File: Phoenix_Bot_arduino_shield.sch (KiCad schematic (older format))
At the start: 14 parts

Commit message: Updated the Schematic with solenoids
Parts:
- removed J?: Conn_01x06_Male, symbol Conn_01x06_Male
- removed Q? (x6): Q_NMOS_GDS, symbol Q_NMOS_GDS
- added J?: Screw_Terminal_01x12, symbol Screw_Terminal_01x12
- added J? (x2): 1x8 Male, symbol Conn_01x08_Male
- added J? (x2): 1x8 Female, symbol Conn_01x08_Female
- added q?: solenoid_1, symbol Q_NMOS_DGS
- added q? (x2): solenoid_3, symbol Q_NMOS_DGS
- added q?: solenoid_4, symbol Q_NMOS_DGS
- added q?: solenoid_5, symbol Q_NMOS_DGS
- added q?: solenoid_6, symbol Q_NMOS_DGS
- J?: value Conn_01x08_Female -> On Board Supply
- J?: value Conn_01x08_Female -> Analog_Pin_1
- J?: value Conn_01x08_Female -> Analog_Pin_2
- J?: value Conn_02x18_Top_Bottom -> Digital_Pins
- J?: value Conn_01x08_Female -> Serial
- J?: value Conn_01x08_Female -> PWM_(6-1)
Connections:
- net labels added: +12V, +5V, 11, 7, 9, Ctrl_1, Ctrl_2, Ctrl_3, Ctrl_4, Ctrl_5, Ctrl_6, Drain_1, Drain_2, Drain_3, Drain_4, Drain_5, Drain_6, RX, TX
- net labels removed: 2, 4, 6
- wire segments 18 -> 87
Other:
- moved on the sheet: J?

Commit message: Updated the Schematic with Analog mapping, encoder, solenoid,  and servo
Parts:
- added J? (x2): Ground, symbol Conn_01x06_Male
- added J?: Servo_Power, symbol Conn_01x06_Male
- added J?: Servo_signal, symbol Conn_01x06_Male
- added J?: PWN(10-5), symbol Conn_01x10_Female
- added J?: ICSP, symbol Conn_02x03_Top_Bottom
- added J?: Encoder_Power, symbol Conn_01x06_Male
- added J?: Encoder_signal, symbol Conn_01x06_Male
- added J?: Analog_signal_female, symbol Conn_01x08_Female
- added J?: Analog_Power_female, symbol Conn_01x08_Female
- added J?: Ground, symbol Conn_01x08_Female
- added J?: Analog_signal_male, symbol Conn_01x08_Male
- added J?: Analog_signal_power, symbol Conn_01x08_Male
- added J?: Ground, symbol Conn_01x08_Male
- J?: value Conn_01x10_Female -> PWN(10-5)
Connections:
- net labels added: +3.3V, AREF, Analog_1, Analog_10, Analog_11, Analog_12, Analog_13, Analog_14, Analog_15, Analog_16, Analog_2, Analog_3, Analog_4, Analog_5, Analog_6, Analog_7, Analog_8, Analog_9, Encoder_1, Encoder_2, Encoder_3, Encoder_4, Encoder_5, Encoder_6, IOREF, Reset, SCL, SDA, Servo_1, Servo_2, Servo_3, Servo_4, Servo_5, Servo_6
- wire segments 87 -> 246

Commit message: Added ICSP mapping
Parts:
- removed J?: ICSP, symbol Conn_02x03_Top_Bottom
- added J?: ICSP, symbol Conn_02x03_Odd_Even
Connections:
- net labels added: MISO, MOSI, SCK, Vcc
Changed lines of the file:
@@
 Servo_6
-$Comp
-L Conn_02x03_Top_Bottom J?
-U 1 1 5A7FF8F4
-P 5950 2350
-F 0 "J?" H 6000 2550 50  0001 C CNN
-F 1 "ICSP" H 6000 2150 50  0000 C CNN
-F 2 "" H 5950 2350 50  0001 C CNN
-F 3 "" H 5950 2350 50  0001 C CNN
-	1    5950 2350
-	1    0    0    -1
-$EndComp
 $Comp
 L GND #PWR?
@@
 Wire Wire Line
 	4900 1450 4900 1500
-Wire Wire Line
-	4900 1450 4900 1500
-Wire Wire Line
-	4800 1450 4800 1500
-Wire Wire Line
-	4700 1450 4700 1500
-Wire Wire Line
-	4600 1450 4600 1500
-Wire Wire Line
-	4500 1450 4500 1500
 Text Label 4900 1500 3    60   ~ 0
 Encoder_1
@@
 Text Label 4900 1500 3    60   ~ 0
 Encoder_1
-Wire Wire Line
-	4400 1450 4400 1500
+$Comp
+L Conn_02x03_Odd_Even J?
+U 1 1 5A80D857
+P 5800 2350
+F 0 "J?" H 5850 2550 50  0001 C CNN
+F 1 "ICSP" H 5850 2150 50  0000 C CNN
+F 2 "" H 5800 2350 50  0001 C CNN
+F 3 "" H 5800 2350 50  0001 C CNN
+	1    5800 2350
+	1    0    0    -1
+$EndComp
+Text Label 5550 2250 2    60   ~ 0
+MISO
+Wire Wire Line
+	5600 2250 5550 2250
+Wire Wire Line
+	5600 2350 5550 2350
+Wire Wire Line
+	5600 2450 5550 2450
+Wire Wire Line
+	6100 2250 6200 2250
+Wire Wire Line
+	6100 2350 6200 2350
+Wire Wire Line
+	6100 2450 6200 2450
+Text Label 5550 2350 2    60   ~ 0
+SCK
+Text Label 5550 2450 2    60   ~ 0
+Reset
+Text Label 6200 2250 0    60   ~ 0
+Vcc
+Text Label 6200 2350 0    60   ~ 0
+MOSI
+$Comp
+L GND #PWR?
+U 1 1 5A80E061
+P 6200 2450
+F 0 "#PWR?" H 6200 2200 50  0001 C CNN
+F 1 "GND" H 6200 2300 50  0000 C CNN
+F 2 "" H 6200 2450 50  0001 C CNN
+F 3 "" H 6200 2450 50  0001 C CNN
+	1    6200 2450
+	0    -1   -1   0
+$EndComp
 $EndSCHEMATC

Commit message: Finished schematic and laid out PCB design
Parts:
- removed J?: PWN(10-5), symbol Conn_01x10_Female
- removed J?: Screw_Terminal_01x12, symbol Screw_Terminal_01x12
- added J27: Solenoid_terminal, Connectors_Terminal_Blocks:TerminalBlock_Altech_AK300-4_P5.00mm, symbol Screw_Terminal_01x04
- added J28: Solendoid_middle_terminal, Connectors_Terminal_Blocks:TerminalBlock_Altech_AK300-4_P5.00mm, symbol Screw_Terminal_01x04
- added J29: bottom_solenoid_terminal, Connectors_Terminal_Blocks:TerminalBlock_Altech_AK300-4_P5.00mm, symbol Screw_Terminal_01x04
- J1, J12, J14, J15, J16, J17, J18, J19, J20, J21, J22, J24, J4, J5, J8, J9: renamed from J?; footprint (none) -> Pin_Headers:Pin_Header_Straight_1x08_Pitch2.54mm
- J10, J11, J2, J3, J6, J7: renamed from J?; footprint (none) -> Pin_Headers:Pin_Header_Straight_1x06_Pitch2.54mm
- J23: renamed from J?; footprint (none) -> Pin_Headers:Pin_Header_Straight_2x03_Pitch2.54mm
- J25: renamed from J?; footprint (none) -> Pin_Headers:Pin_Header_Straight_2x18_Pitch2.54mm
- q1, q2, q3, q4, q5, q6: renamed from q?; footprint (none) -> TO_SOT_Packages_THT:TO-220-3_Vertical

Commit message: Fixed hole alignment and pin count issues
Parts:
- J14: footprint Pin_Headers:Pin_Header_Straight_1x08_Pitch2.54mm -> Pin_Headers:Pin_Header_Straight_1x10_Pitch2.54mm
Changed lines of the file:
@@
 LIBS:contrib
 LIBS:valves
-LIBS:Phoenix_Bot_arduino_shield-cache
 EELAYER 25 0
 EELAYER END
@@
 F 0 "J14" H 3850 1950 50  0001 C CNN
 F 1 "PWN(10-5)" H 3850 850 50  0001 C CNN
-F 2 "Pin_Headers:Pin_Header_Straight_1x08_Pitch2.54mm" H 3850 1450 50  0001 C CNN
+F 2 "Pin_Headers:Pin_Header_Straight_1x10_Pitch2.54mm" H 3850 1450 50  0001 C CNN
 F 3 "" H 3850 1450 50  0001 C CNN
 	1    3850 1450

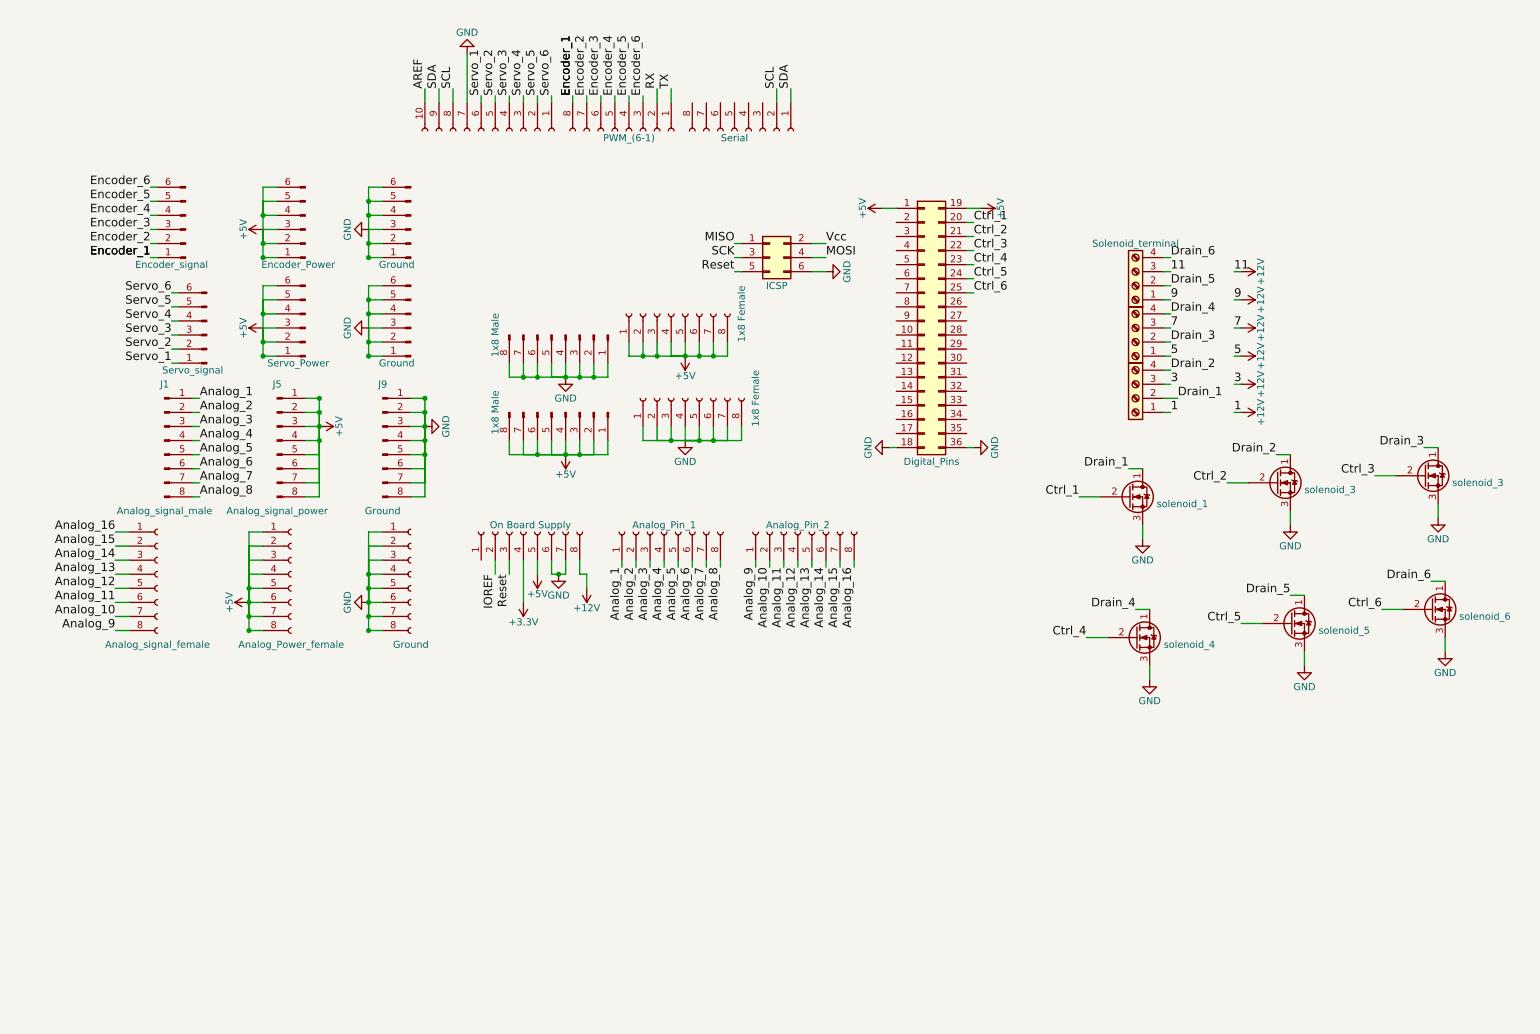
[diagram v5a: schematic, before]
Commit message: Fixed issues porting from mac and started solenoid wiring
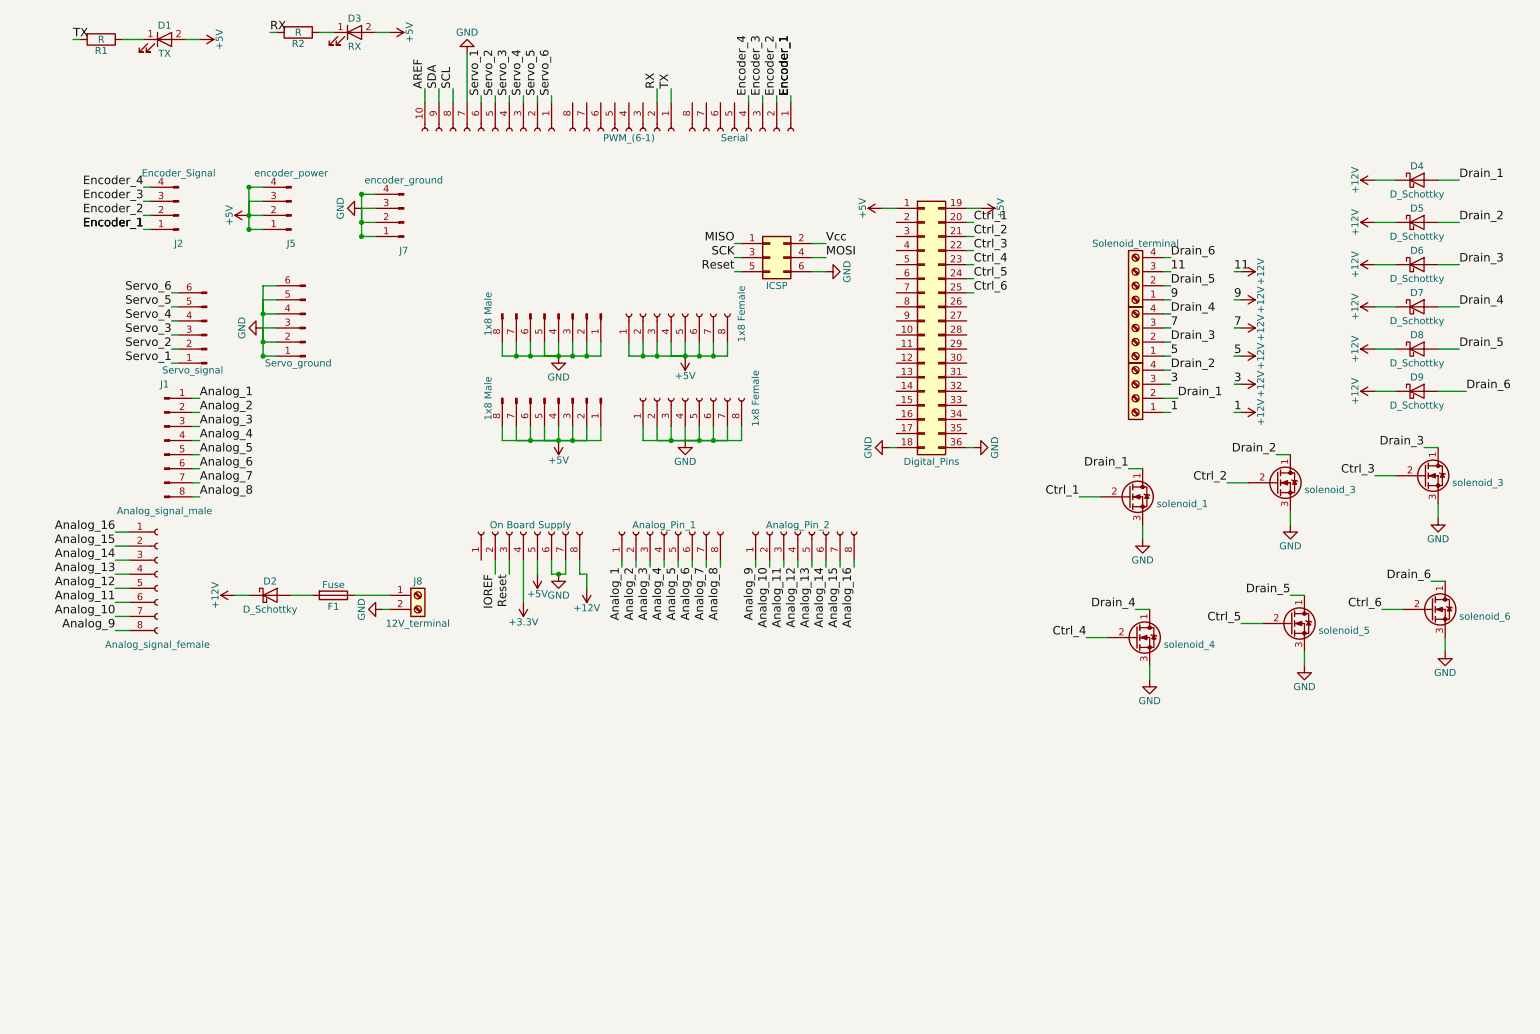
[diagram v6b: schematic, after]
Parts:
- removed J10, J11: Ground, Pin_Headers:Pin_Header_Straight_1x06_Pitch2.54mm, symbol Conn_01x06_Male
- removed J12: Ground, Pin_Headers:Pin_Header_Straight_1x08_Pitch2.54mm, symbol Conn_01x08_Female
- removed J2: Encoder_signal, Pin_Headers:Pin_Header_Straight_1x06_Pitch2.54mm, symbol Conn_01x06_Male
- removed J5: Analog_signal_power, Pin_Headers:Pin_Header_Straight_1x08_Pitch2.54mm, symbol Conn_01x08_Male
- removed J7: Encoder_Power, Pin_Headers:Pin_Header_Straight_1x06_Pitch2.54mm, symbol Conn_01x06_Male
- removed J8: Analog_Power_female, Pin_Headers:Pin_Header_Straight_1x08_Pitch2.54mm, symbol Conn_01x08_Female
- removed J9: Ground, Pin_Headers:Pin_Header_Straight_1x08_Pitch2.54mm, symbol Conn_01x08_Male
- added D1: TX, LEDs:LED_0805_HandSoldering, symbol LED
- added D2: D_Schottky, TO_SOT_Packages_THT:TO-220-2_Vertical, symbol D_Schottky
- added D3: RX, LEDs:LED_0805_HandSoldering, symbol LED
- added D4, D5, D6, D7, D8, D9: D_Schottky, Diodes_SMD:D_SMC, symbol D_Schottky
- added F1: Fuse, Pin_Headers:Pin_Header_Straight_1x03_Pitch2.54mm, symbol Fuse
- added J2: Encoder_Signal, Pin_Headers:Pin_Header_Straight_1x04_Pitch2.54mm, symbol Conn_01x04_Male
- added J5: encoder_power, Pin_Headers:Pin_Header_Straight_1x04_Pitch2.54mm, symbol Conn_01x04_Male
- added J7: encoder_ground, Pin_Headers:Pin_Header_Straight_1x04_Pitch2.54mm, symbol Conn_01x04_Male
- added J8: 12V_terminal, TerminalBlock:TerminalBlock_Altech_AK300-2_P5.00mm, symbol Screw_Terminal_01x02
- added R1, R2: R, Resistors_SMD:R_0805_HandSoldering, symbol R
- J6: value Servo_Power -> Servo_ground
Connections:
- net +12V: now also D2.1 (K), D4.1 (K), D5.1 (K), D6.1 (K), D7.1 (K), D8.1 (K), D9.1 (K)
- net +5V: now also D1.2 (A), D3.2 (A), J5.1 (Pin_1), J5.2 (Pin_2), J5.3 (Pin_3), J5.4 (Pin_4); no longer J6.1 (Pin_1), J6.2 (Pin_2), J6.3 (Pin_3), J6.4 (Pin_4), J6.5 (Pin_5), J6.6 (Pin_6)
- net Drain_1: now also D4.2 (A)
- net Drain_2: now also D5.2 (A)
- net Drain_3: now also D6.2 (A)
- net Drain_4: now also D7.2 (A)
- net Drain_5: now also D8.2 (A)
- net Drain_6: now also D9.2 (A)
- net Encoder_1: now also J22.1 (Pin_1), J2.1 (Pin_1); no longer J18.8 (Pin_8)
- net Encoder_2: now also J22.2 (Pin_2), J2.2 (Pin_2); no longer J18.7 (Pin_7)
- net Encoder_3: now also J22.3 (Pin_3), J2.3 (Pin_3); no longer J18.6 (Pin_6)
- net Encoder_4: now also J22.4 (Pin_4), J2.4 (Pin_4); no longer J18.5 (Pin_5)
- net GND: now also J6.1 (Pin_1), J6.2 (Pin_2), J6.3 (Pin_3), J6.4 (Pin_4), J6.5 (Pin_5), J6.6 (Pin_6), J7.1 (Pin_1), J7.2 (Pin_2), J7.3 (Pin_3), J7.4 (Pin_4), J8.2 (Pin_2)
- net RX: now also R2.2
- net SCL: no longer J22.2 (Pin_2)
- net SDA: no longer J22.1 (Pin_1)
- net TX: now also R1.2
- net Encoder_5: no longer names the net of J18.4 (Pin_4)
- net Encoder_6: no longer names the net of J18.3 (Pin_3)
- new net: D1.1 (K), R1.1
- new net: D3.1 (K), R2.1
- new net: D2.2 (A), F1.2
- new net: F1.1, J8.1 (Pin_1)
